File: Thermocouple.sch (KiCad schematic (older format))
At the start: 0 parts

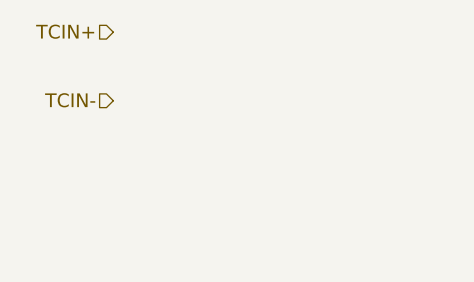
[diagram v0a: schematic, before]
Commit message: added inputs and outputs
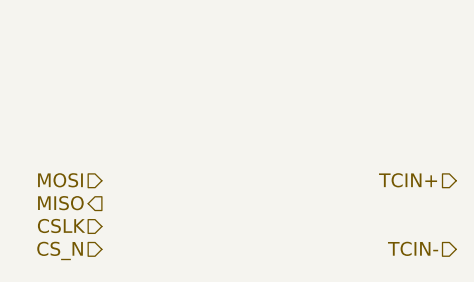
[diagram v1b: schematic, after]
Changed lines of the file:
@@
 Comment4 ""
 $EndDescr
-Text HLabel 2500 1950 0    60   Input ~ 0
+Text HLabel 4000 2600 0    60   Input ~ 0
 TCIN+
-Text HLabel 2500 2250 0    60   Input ~ 0
+Text HLabel 4000 2900 0    60   Input ~ 0
 TCIN-
+Text HLabel 2450 2600 0    60   Input ~ 0
+MOSI
+Text HLabel 2450 2700 0    60   Output ~ 0
+MISO
+Text HLabel 2450 2800 0    60   Input ~ 0
+CSLK
+Text HLabel 2450 2900 0    60   Input ~ 0
+CS_N
 $EndSCHEMATC
